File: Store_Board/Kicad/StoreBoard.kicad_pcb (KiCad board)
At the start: 2 copper layers, 230 x 78 mm, 36 parts, among them J1 Conn_01x10, J2 Conn_01x10, J3 Conn_01x10, J4 Conn_01x10, U1 HM62256BLP, U2 74HCT574, U3 74HCT574, U4 74HCT04, U417 74LS00, U418 74LS00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

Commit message: Ready for testing, I think
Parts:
- removed RN2: 33, Package_DIP:DIP-18_W7.62mm_Socket
- added HOLE1: HOLE, MountingHole:MountingHole_3.2mm_M3_Pad, F.Cu at (236.7, 59.2)
- added HOLE2: HOLE, MountingHole:MountingHole_3.2mm_M3_Pad, F.Cu at (142.7, 101.7)
- added RN53: 33, Package_DIP:DIP-18_W7.62mm, F.Cu at (201.5, 81.2)
- R46, R50, R56: footprint Resistor_THT:R_Axial_DIN0204_L3.6mm_D1.6mm_P2.54mm_Vertical -> Resistor_THT:R_Axial_DIN0204_L3.6mm_D1.6mm_P5.08mm_Horizontal
- RN52: footprint Package_DIP:DIP-16_W7.62mm_Socket -> Package_DIP:DIP-16_W7.62mm
- moved C14 34.0 mm to (194.8, 130.3)
- moved C59 33.1 mm to (219.6, 130.2)
- moved C58 32.2 mm to (208.2, 130.3)
- moved J2 31.4 mm to (245.3, 98.9)
- moved J3 31.4 mm to (237.8, 68.0)
- moved J1 31.4 mm to (245.1, 68.1)
- moved J4 31.4 mm to (237.4, 99.1)
- moved U417 30.8 mm to (146.2, 125.7)
- moved U418 30.0 mm to (158.7, 125.7)
- moved U420 29.5 mm to (182.0, 125.7)
- moved U419 29.5 mm to (170.7, 125.7)
- moved U421 29.5 mm to (193.3, 125.7)
- moved U422 29.5 mm to (205.3, 125.7)
- moved C49 28.8 mm to (174.4, 99.7)
- moved C5 28.8 mm to (138.7, 60.0)
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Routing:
- net /RAS_A14: track 156.9 -> 64.6 mm, vias 0 -> 2
- net /RAS_A2: track 127.6 -> 71.6 mm
- net /TVAD: track 137.7 -> 168.2 mm, vias 2 -> 0
- net /1\4: track 105.9 -> 130.8 mm, vias 1 -> 2
- net /~{RD}: track 57.6 -> 33.3 mm
- net Net-(U421B-~{R}): track 66.7 -> 43.5 mm
- net Net-(U421A-~{Q}): track 43.7 -> 65.6 mm, vias 0 -> 1
- net VCC: track 424.0 -> 403.8 mm, vias 1 -> 2
- net /~{TVCLK}: track 83.1 -> 63.7 mm, vias 1 -> 0
- net /1\2: track 104.3 -> 85.0 mm, vias 1 -> 0
- net Net-(U1-~{WE}): track 47.4 -> 66.7 mm, vias 3 -> 0
- net /ZCK: track 93.2 -> 111.6 mm
- net /A1: track 119.7 -> 101.3 mm, vias 1 -> 0
- net Net-(C57-Pad1): track 18.1 -> 36.1 mm
- net /RAS_A1: track 68.0 -> 83.3 mm
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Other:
- board size 230 x 78 mm -> 145 x 78 mm

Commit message: Added testpoints
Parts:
- added TP1: Conn_01x04_Pin, Connector_PinHeader_2.54mm:PinHeader_1x04_P2.54mm_Vertical, F.Cu at (145.1, 60.0)
- C11, C14, C17, C2, C20, C23, C5, C55, C58, C59, C8: value 0.1 -> 100nF
- C28: value 10uf 35v -> 110µF 35v
- C49, C57: value 220pf -> 220pF
- R46, R56: value 150 -> 150Ω
- R50, RN52, RN53: value 33 -> 33Ω
- RN54: value 4K7 -> 4.7KΩ
- moved C49 3.99 mm to (170.5, 100.3)
- moved R46 3.99 mm to (166.8, 100.1)
- turned HOLE1 to -90 degrees
- turned HOLE2 to -90 degrees
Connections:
- net Net-(U2-Cp) renamed /RAS16A
- net Net-(U3-Cp) renamed /RAS32A
- net Net-(U417-Pad1) renamed /A14M
- HOLE1 pad 1: unconnected-(HOLE1-Pad1) -> GND
- HOLE2 pad 1: unconnected-(HOLE2-Pad1) -> GND
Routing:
- net /A14M: track 32.4 -> 106.9 mm, vias 0 -> 1
- net /~{CAS}: track 4.53 -> 47.7 mm
- net /A5: track 135.9 -> 99.2 mm, vias 0 -> 2
- net /1\4: track 130.8 -> 96.4 mm, vias 2 -> 1
- net /RAS_A3: track 75.7 -> 102.6 mm, vias 0 -> 1
- net /RAS16A: track 58.9 -> 80.3 mm
- net /M1,4: track 40.2 -> 55.3 mm
- net /1\2: track 85.0 -> 70.0 mm
- net Net-(U421B-~{R}): track 43.5 -> 30.1 mm, vias 1 -> 0
- net /RAS_A1: track 83.3 -> 70.3 mm, vias 0 -> 1
- net Net-(U1-~{WE}): track 66.7 -> 54.4 mm
- net /A3: track 105.4 -> 115.7 mm, vias 0 -> 1
- net /~{RD}: track 33.3 -> 43.5 mm
- net /ROW: track 85.4 -> 94.6 mm, vias 0 -> 1
- net /~{TVCLK}: track 63.7 -> 55.3 mm
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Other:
- board text added: "TP_A14M"
- board text added: "TP_RAS16A"
- board text added: "TP_RAS32A"
- board text added: "TP_~{CAS}"

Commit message: Further refinements
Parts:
- removed R50: 33Ω, Resistor_THT:R_Axial_DIN0204_L3.6mm_D1.6mm_P5.08mm_Horizontal
- removed RN52: 33Ω, Package_DIP:DIP-16_W7.62mm
- removed RN53: 33Ω, Package_DIP:DIP-18_W7.62mm
- C28: value 110µF 35v -> 10µF 35v
- TP1: value Conn_01x04_Pin -> Conn_02x05_Odd_Even; footprint Connector_PinHeader_2.54mm:PinHeader_1x04_P2.54mm_Vertical -> Connector_PinHeader_2.54mm:PinHeader_2x05_P2.54mm_Vertical
- U2: value 74HCT574 -> 74LS574
- U3: value 74HCT574 -> 74LS32; footprint Package_DIP:DIP-20_W7.62mm -> Package_DIP:DIP-14_W7.62mm
- U4: value 74HCT04 -> 74LS04
- U420: value 74HC04 -> 74LS04
- moved C5 84.3 mm to (221.2, 77.4), turned to 90 degrees
- moved U3 82.4 mm to (215.8, 72.7), turned to -90 degrees
- moved C11 43.1 mm to (195.0, 79.8)
- moved U4 36.2 mm to (200.4, 66.7)
- moved C8 36.2 mm to (194.4, 64.5)
- moved RN54 30.2 mm to (149.5, 68.5), turned to -90 degrees
- moved C2 30.0 mm to (195.5, 90.1)
- moved U2 29.9 mm to (200.4, 95.2)
- moved TP1 14.9 mm to (158.1, 67.3), turned to 180 degrees
- moved R56 6.91 mm to (177.0, 100.6)
- moved C57 6.47 mm to (185.8, 100.6)
- moved C49 2.04 mm to (172.5, 100.7), turned to 180 degrees
- moved R46 1.55 mm to (165.3, 100.5)
- moved U1 1.34 mm to (190.1, 71.0)
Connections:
- RN54 pad 1: VCC -> unconnected-(RN54-common-Pad1)
- RN54 pad 2: /D7 -> /M4,6
- RN54 pad 3: /D6 -> /M4,7
- RN54 pad 4: /D5 -> /M4,8
- RN54 pad 5: /D4 -> /M1,1
- RN54 pad 6: /D3 -> /M4,10
- RN54 pad 7: /D2 -> /M2,10
- RN54 pad 8: /D1 -> /M4,9
- RN54 pad 9: /D0 -> /M4,3
- TP1 pad 2: /~{CAS} -> GND
- TP1 pad 3: /RAS16A -> /~{CAS}
- TP1 pad 4: /RAS32A -> GND
- U1 pad 1: /RAS_A14 -> /A14M
- U1 pad 11: /D0 -> /M4,6
- U1 pad 12: /D1 -> /M4,7
- U1 pad 13: /D2 -> /M4,8
- U1 pad 15: /D3 -> /M1,1
- U1 pad 16: /D4 -> /M4,10
- U1 pad 17: /D5 -> /M2,10
- U1 pad 18: /D6 -> /M4,9
- U1 pad 19: /D7 -> /M4,3
- U2 pad 11: /RAS16A -> /RAS
- U3 pad 1: GND -> /RAS16
- U3 pad 11: /RAS32A -> unconnected-(U3-Pad11)
- U3 pad 12: /RAS_A14 -> GND
- U3 pad 13: /RAS_A6 -> GND
- U3 pad 14: /RAS_A5 -> VCC
- U3 pad 2: /A0 -> /RAS32
- U3 pad 3: /A1 -> /RAS
- U3 pad 4: /A2 -> GND
- U3 pad 5: /A3 -> GND
- U3 pad 6: /A4 -> unconnected-(U3-Pad6)
- U3 pad 7: /A5 -> GND
- U3 pad 8: /A6 -> unconnected-(U3-Pad8)
- U3 pad 9: /RAS32A -> GND
- U4 pad 1: /~{RAS16A} -> /~{RAS16}
- U4 pad 2: /RAS16A -> /RAS16
- U4 pad 3: /~{RAS32A} -> (no net)
- U4 pad 4: /RAS32A -> (no net)
- U4 pad 5: GND -> /~{RAS32}
- U4 pad 6: unconnected-(U4-Pad6) -> /RAS32
- U421 pad 7: Net-(U421B-~{Q}) -> /~{CAS}
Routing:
- net /M4,8: track 31.7 -> 177.8 mm
- net VCC: track 408.7 -> 284.4 mm, vias 0 -> 1
- net /M4,6: track 24.0 -> 141.1 mm, vias 0 -> 1
- net /D0: track 115.6 -> 0.00 mm
- net /D1: track 106.5 -> 0.00 mm
- net /D2: track 94.9 -> 0.00 mm
- net /M4,7: track 27.5 -> 112.4 mm, vias 0 -> 2
- net /M4,10: track 42.1 -> 123.9 mm
- net /RAS16A: track 80.3 -> 0.00 mm
- net /RAS: track 0.00 -> 78.4 mm
- net /A3: track 115.7 -> 43.6 mm, vias 1 -> 0
- net /A1: track 99.1 -> 27.1 mm, vias 1 -> 0
- net /D3: track 69.1 -> 0.00 mm
- net /A6: track 105.0 -> 37.2 mm
- net /A2: track 100.3 -> 33.1 mm, vias 1 -> 0
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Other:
- board size 145 x 78 mm -> 115 x 78 mm
- board text added: "GND"
- board text added: "TP_RAS"
- board text added: "TP_RAS16"
- board text added: "TP_RAS32"
- board text removed: "TP_RAS16A"
- board text removed: "TP_RAS32A"

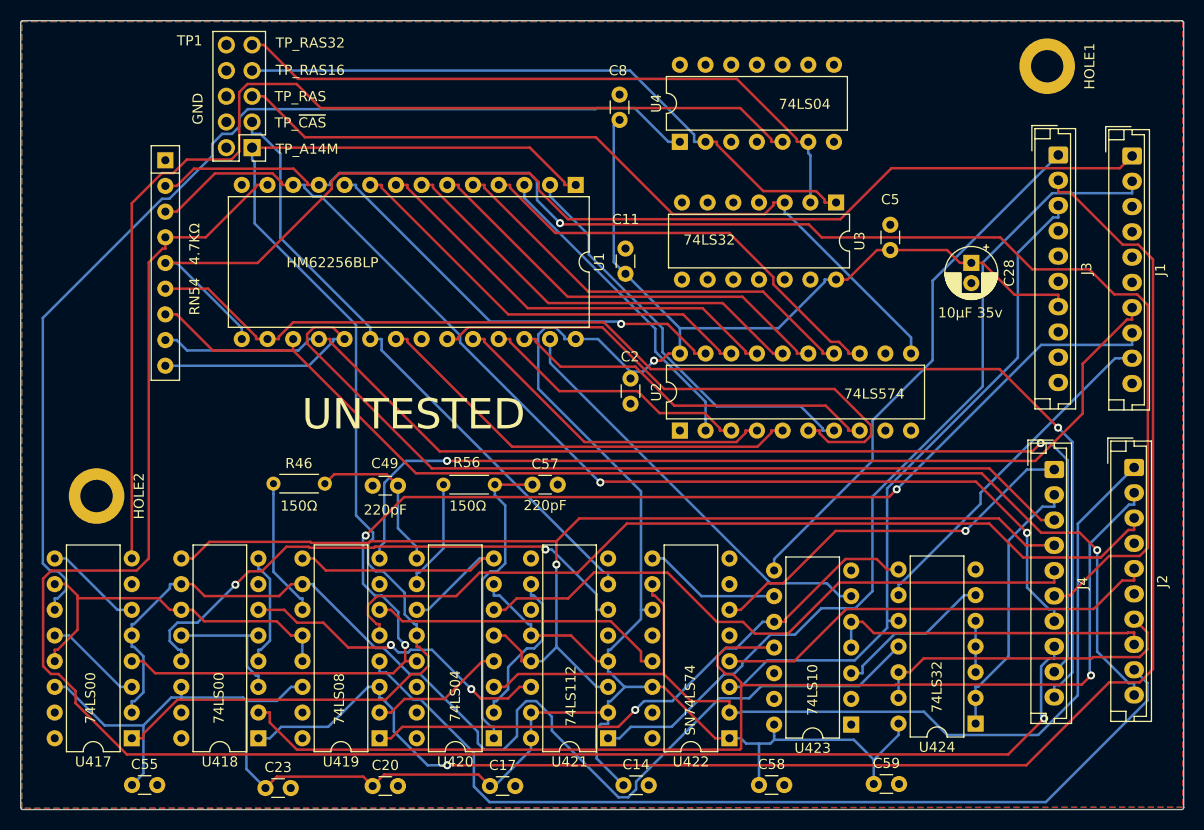
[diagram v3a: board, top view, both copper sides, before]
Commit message: Further refinements to RAS handling
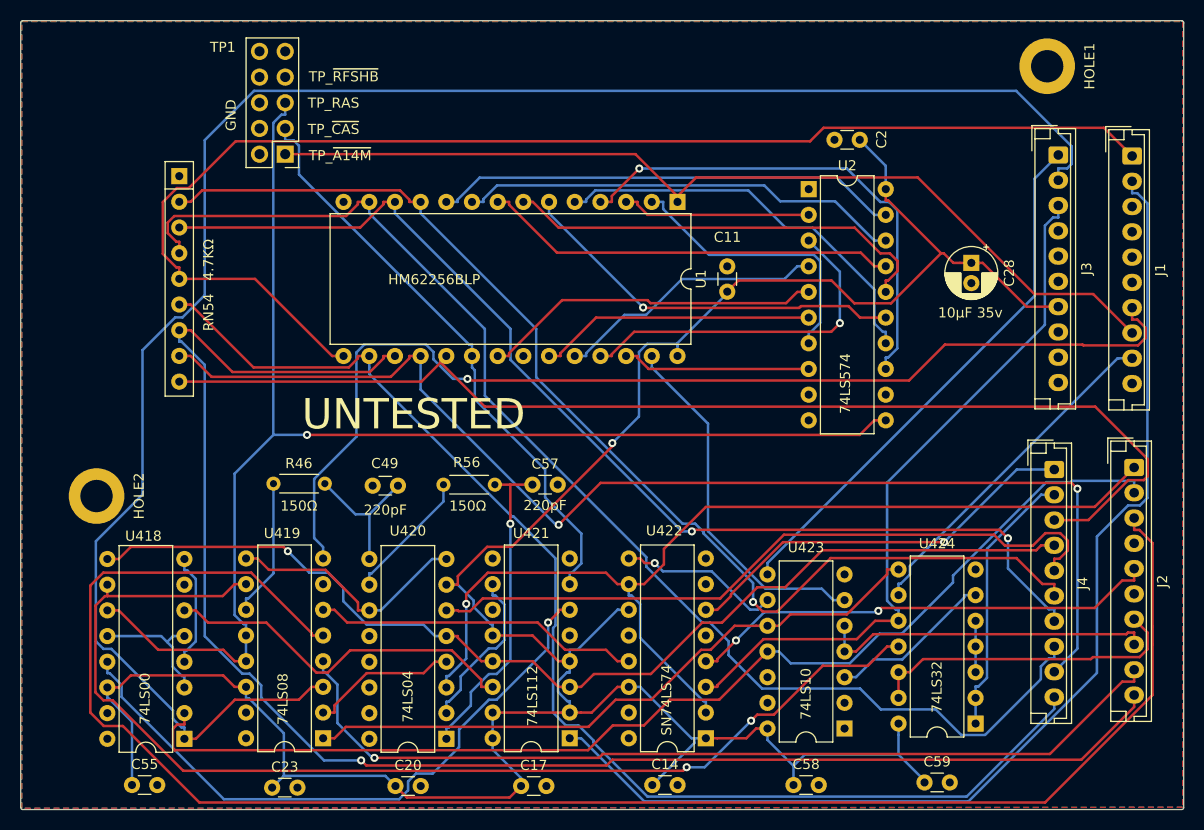
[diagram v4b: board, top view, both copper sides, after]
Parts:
- removed C5, C8: 100nF, Capacitor_THT:C_Disc_D3.0mm_W1.6mm_P2.50mm
- removed U3: 74LS32, Package_DIP:DIP-14_W7.62mm
- removed U4: 74LS04, Package_DIP:DIP-14_W7.62mm
- removed U417: 74LS00, Package_DIP:DIP-16_W7.62mm
- moved C2 32.7 mm to (218.2, 66.5), turned to 180 degrees
- moved U2 27.1 mm to (213.1, 71.4), turned to 0 degrees
- moved C11 10.2 mm to (205.1, 81.5)
- moved U1 10.2 mm to (200.1, 72.6)
- moved U418 7.32 mm to (151.4, 125.7)
- moved U419 5.58 mm to (165.1, 125.7)
- moved C59 5.02 mm to (224.6, 130.0)
- moved U420 4.69 mm to (177.3, 125.7)
- moved U421 3.80 mm to (189.5, 125.7)
- moved C58 3.41 mm to (211.6, 130.3)
- moved TP1 3.34 mm to (161.4, 67.9)
- moved C17 3.08 mm to (184.7, 130.4)
- moved C14 2.85 mm to (197.7, 130.3)
- moved U422 2.33 mm to (202.9, 125.7)
- moved C20 2.25 mm to (172.3, 130.4)
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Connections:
- TP1 pad 1: /A14M -> /~{A14M}
- TP1 pad 7: /RAS16 -> /~{RFSHB}
- TP1 pad 9: /RAS32 -> unconnected-(TP1-Pin_9-Pad9)
- U1 pad 1: /A14M -> /~{A14M}
- U418 pad 11: Net-(U417-Pad10) -> /RAS
- U419 pad 12: Net-(U417-Pad10) -> /RAS
- U419 pad 13: Net-(U417-Pad10) -> /RAS
- U420 pad 12: /A14M -> (no net)
- U420 pad 13: /~{A14M} -> (no net)
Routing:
- net /A14M: track 125.8 -> 0.00 mm
- net /~{RAS32}: track 110.3 -> 0.00 mm
- net /~{RAS16}: track 105.1 -> 0.00 mm
- net /FRM: track 86.4 -> 170.5 mm
- net /RAS32: track 65.2 -> 0.00 mm
- net /RAS16: track 63.9 -> 0.00 mm
- net /RAS: track 78.4 -> 135.1 mm, vias 0 -> 1
- net /M4,8: track 177.8 -> 125.1 mm, vias 1 -> 0
- net /M2,10: track 119.1 -> 156.7 mm
- net Net-(U417-Pad10): track 36.6 -> 0.00 mm
- net /~{A14M}: track 128.6 -> 93.2 mm, vias 3 -> 0
- net /A4: track 55.8 -> 27.4 mm
- net /M4,6: track 141.1 -> 113.5 mm
- net /TVAD: track 153.4 -> 178.6 mm, vias 1 -> 0
- net /ZCK: track 88.1 -> 112.3 mm
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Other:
- board text added: "TP_~{A14M}"
- board text added: "TP_~{RFSHB}"
- board text removed: "TP_A14M"
- board text removed: "TP_RAS16"
- board text removed: "TP_RAS32"

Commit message: Final update before test fabrication
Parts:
- added RN1: 33Ω, Package_DIP:DIP-16_W7.62mm, F.Cu at (220.7, 58.9)
- added RN2: 33Ω, Package_DIP:DIP-16_W7.62mm, F.Cu at (202.4, 83.8)
- moved C11 8.91 mm to (196.2, 82.3)
- moved U1 8.91 mm to (191.3, 73.4)
- moved U2 8.19 mm to (215.4, 79.2)
- moved C2 7.88 mm to (220.0, 74.2)
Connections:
- RN54 pad 2: /M4,6 -> /D0
- RN54 pad 3: /M4,7 -> /D1
- RN54 pad 4: /M4,8 -> /D2
- RN54 pad 5: /M1,1 -> /D3
- RN54 pad 6: /M4,10 -> /D4
- RN54 pad 7: /M2,10 -> /D5
- RN54 pad 8: /M4,9 -> /D6
- RN54 pad 9: /M4,3 -> /D7
- TP1 pad 7: /~{RFSHB} -> /~{RFRSHB}
- TP1 pad 9: unconnected-(TP1-Pin_9-Pad9) -> /ROW
- U1 pad 11: /M4,6 -> /D0
- U1 pad 12: /M4,7 -> /D1
- U1 pad 13: /M4,8 -> /D2
- U1 pad 15: /M1,1 -> /D3
- U1 pad 16: /M4,10 -> /D4
- U1 pad 17: /M2,10 -> /D5
- U1 pad 18: /M4,9 -> /D6
- U1 pad 19: /M4,3 -> /D7
- U421 pad 7: /~{CAS} -> /~{CAS}_PRE
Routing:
- net /M2,10: track 156.7 -> 57.6 mm
- net /D3: track 0.00 -> 78.6 mm, vias 0 -> 1
- net /M4,3: track 114.4 -> 36.7 mm
- net /D4: track 0.00 -> 76.4 mm, vias 0 -> 1
- net /M4,8: track 125.1 -> 53.3 mm, vias 0 -> 1
- net /~{CAS}_PRE: track 0.00 -> 70.3 mm, vias 0 -> 1
- net /D2: track 0.00 -> 68.0 mm
- net /D1: track 0.00 -> 66.6 mm
- net /D7: track 0.00 -> 66.0 mm
- net /D5: track 0.00 -> 65.4 mm
- net /D0: track 0.00 -> 65.2 mm
- net /D6: track 0.00 -> 65.1 mm, vias 0 -> 2
- net /M4,9: track 120.5 -> 56.3 mm, vias 2 -> 0
- net /ROW: track 108.4 -> 170.4 mm, vias 1 -> 0
- net /M4,10: track 122.9 -> 64.3 mm, vias 0 -> 2
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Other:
- board text added: "TP_ROW"
- board text added: "TP_~{RFRSHB}"
- board text removed: "TP_~{RFSHB}"
- board text removed: "UNTESTED"

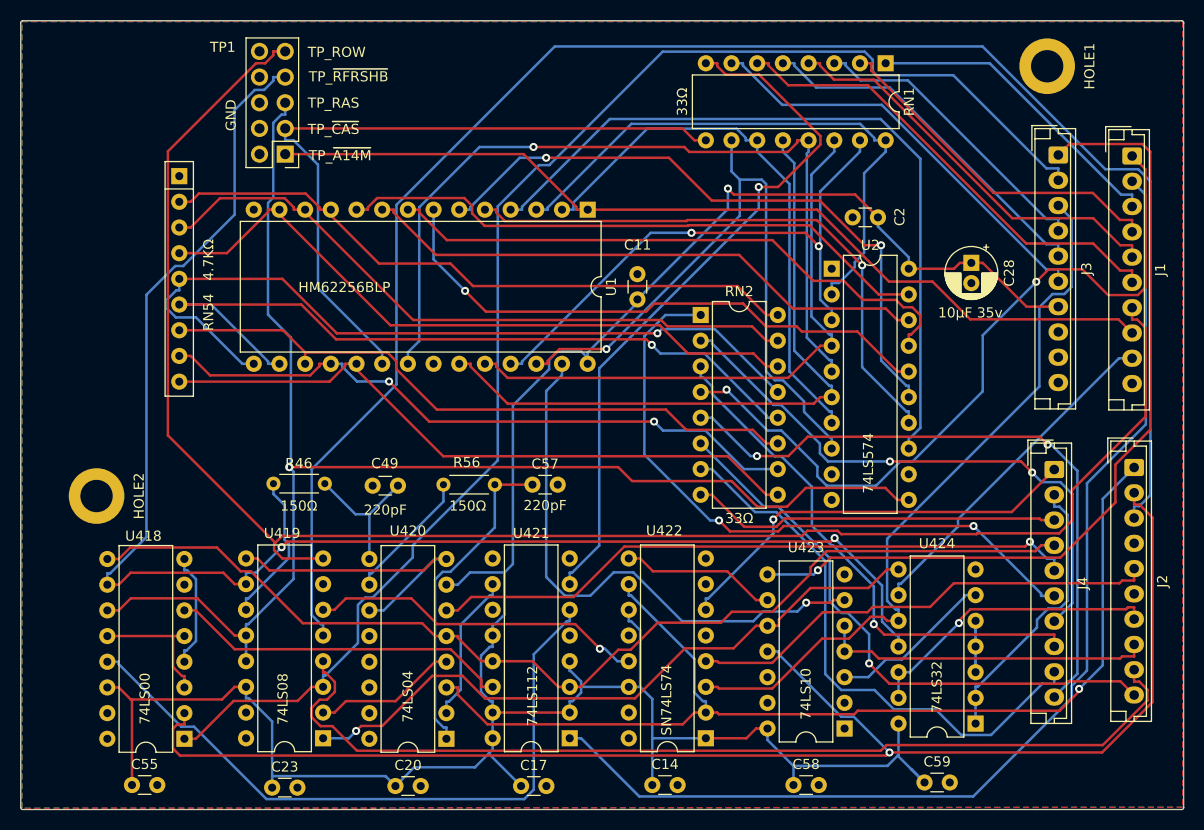
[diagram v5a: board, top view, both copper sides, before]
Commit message: Corrected footprints
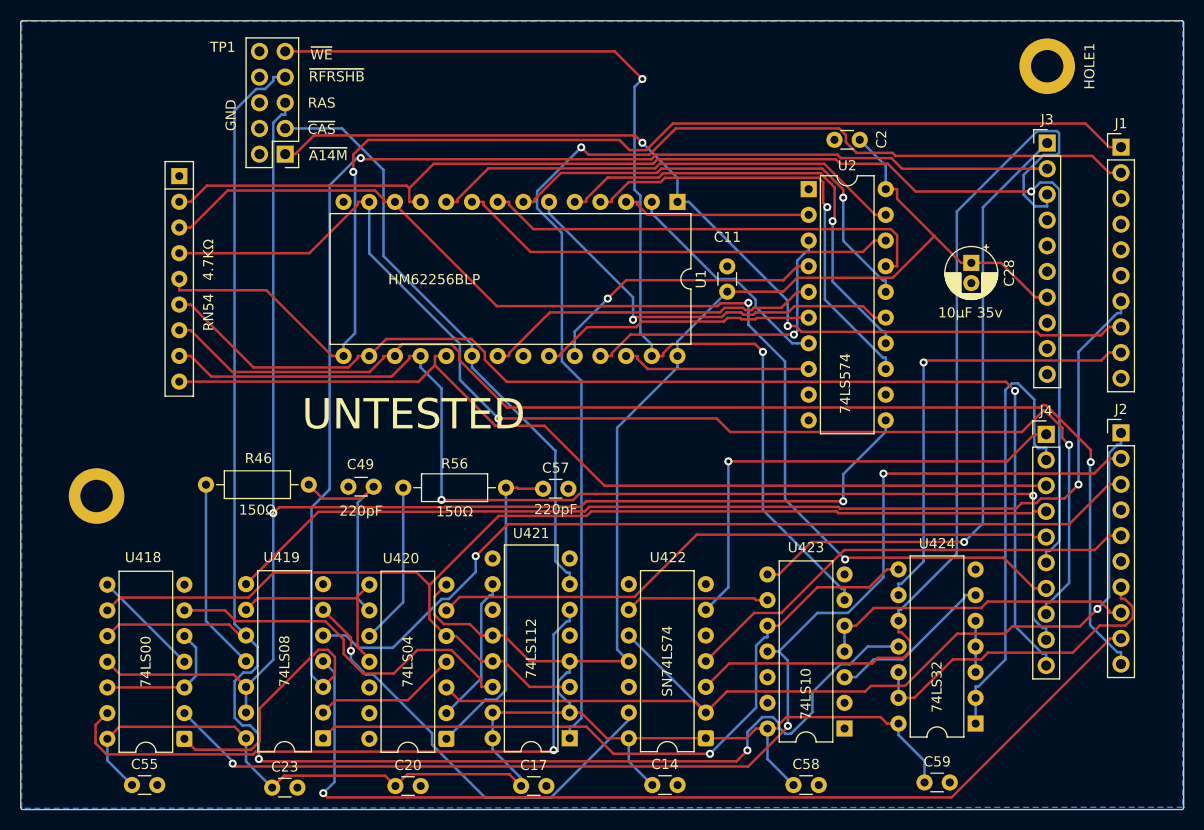
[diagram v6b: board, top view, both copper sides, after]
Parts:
- removed RN1, RN2: 33Ω, Package_DIP:DIP-16_W7.62mm
- J1, J2, J3, J4: footprint Connector_JST:JST_EH_B10B-EH-A_1x10_P2.50mm_Vertical -> Connector_PinHeader_2.54mm:PinHeader_1x10_P2.54mm_Vertical
- R46, R56: footprint Resistor_THT:R_Axial_DIN0204_L3.6mm_D1.6mm_P5.08mm_Horizontal -> Resistor_THT:R_Axial_DIN0207_L6.3mm_D2.5mm_P10.16mm_Horizontal
- U418, U419, U420, U422: footprint Package_DIP:DIP-16_W7.62mm -> Package_DIP:DIP-14_W7.62mm
- moved C11 8.91 mm to (205.1, 81.5)
- moved U1 8.91 mm to (200.1, 72.6)
- moved U2 8.19 mm to (213.1, 71.4)
- moved C2 7.88 mm to (218.2, 66.5)
- moved R56 3.99 mm to (173.0, 100.9)
- moved J2 3.66 mm to (244.0, 95.5), turned to 0 degrees
- moved J4 3.57 mm to (236.6, 95.6), turned to 0 degrees
- moved C49 2.40 mm to (170.1, 100.8)
- moved J3 1.61 mm to (236.7, 66.8), turned to 0 degrees
- moved R46 1.59 mm to (163.7, 100.6)
- moved J1 1.41 mm to (244.0, 67.2), turned to 0 degrees
- moved C57 1.12 mm to (186.8, 101.0)
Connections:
- RN54 pad 2: /D0 -> /M4,6
- RN54 pad 3: /D1 -> /M4,7
- RN54 pad 4: /D2 -> /M4,8
- RN54 pad 5: /D3 -> /M1,1
- RN54 pad 6: /D4 -> /M4,10
- RN54 pad 7: /D5 -> /M2,10
- RN54 pad 8: /D6 -> /M4,9
- RN54 pad 9: /D7 -> /M4,3
- TP1 pad 9: /ROW -> /~{WE}
- U1 pad 11: /D0 -> /M4,6
- U1 pad 12: /D1 -> /M4,7
- U1 pad 13: /D2 -> /M4,8
- U1 pad 15: /D3 -> /M1,1
- U1 pad 16: /D4 -> /M4,10
- U1 pad 17: /D5 -> /M2,10
- U1 pad 18: /D6 -> /M4,9
- U1 pad 19: /D7 -> /M4,3
- U1 pad 27: Net-(U1-~{WE}) -> /~{WE}
- U421 pad 7: /~{CAS}_PRE -> /~{CAS}
- U423 pad 6: Net-(U1-~{WE}) -> /~{WE}
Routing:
- net /~{WE}: track 0.00 -> 104.9 mm, vias 0 -> 2
- net /FRM: track 168.1 -> 87.0 mm, vias 0 -> 1
- net /D3: track 78.6 -> 0.00 mm, vias 1 -> 0
- net /D4: track 76.4 -> 0.00 mm, vias 1 -> 0
- net /M4,8: track 53.3 -> 125.5 mm, vias 1 -> 2
- net /~{CAS}_PRE: track 70.3 -> 0.00 mm, vias 1 -> 0
- net /D2: track 68.0 -> 0.00 mm
- net /D1: track 66.6 -> 0.00 mm
- net /M4,6: track 65.0 -> 131.1 mm, vias 2 -> 1
- net /D7: track 66.0 -> 0.00 mm
- net /D5: track 65.4 -> 0.00 mm
- net /D0: track 65.2 -> 0.00 mm
- net /D6: track 65.1 -> 0.00 mm, vias 2 -> 0
- net /ROW: track 170.4 -> 106.6 mm, vias 0 -> 1
- net /M2,10: track 57.6 -> 121.2 mm
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- removed copper zone on F.Cu, net GND
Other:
- board text added: "RAS"
- board text added: "UNTESTED"
- board text added: "~{A14M}"
- board text added: "~{CAS}"
- board text added: "~{RFRSHB}"
- board text added: "~{WE}"
- board text removed: "TP_RAS"
- board text removed: "TP_ROW"
- board text removed: "TP_~{A14M}"
- board text removed: "TP_~{CAS}"
- board text removed: "TP_~{RFRSHB}"
